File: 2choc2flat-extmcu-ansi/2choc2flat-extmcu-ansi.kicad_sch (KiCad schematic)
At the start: 142 parts, among them J1 Conn_01x09_Male, J2 Conn_01x05_Male, J3 Conn_01x09_Male, K1 KEYSW, K10 KEYSW, K11 KEYSW, K12 KEYSW, K13 KEYSW, K14 KEYSW, K16 KEYSW, K17 KEYSW, K18 KEYSW, K19 KEYSW, K2 KEYSW, K20 KEYSW, K21 KEYSW, K22 KEYSW, K23 KEYSW, K24 KEYSW, K25 KEYSW, K26 KEYSW, K27 KEYSW, K28 KEYSW, K29 KEYSW, K3 KEYSW, K31 KEYSW, K31-1 KEYSW, K32 KEYSW, K33 KEYSW, K34 KEYSW, K35 KEYSW, K36 KEYSW, K37 KEYSW, K38 KEYSW, K39 KEYSW, K4 KEYSW, K40 KEYSW, K41 KEYSW, K42 KEYSW, K44 KEYSW, K46 KEYSW, K47 KEYSW, K48 KEYSW, K49 KEYSW, K5 KEYSW, K50 KEYSW, K51 KEYSW, K52 KEYSW, K53 KEYSW, K54 KEYSW, K55 KEYSW, K56 KEYSW, K57 KEYSW, K58 KEYSW, K59 KEYSW, K6 KEYSW, K61 KEYSW, K62 KEYSW, K63 KEYSW, K67 KEYSW, K7 KEYSW, K71 KEYSW, K72 KEYSW, K73 KEYSW, K74 KEYSW, K75 KEYSW, K8 KEYSW, K9 KEYSW

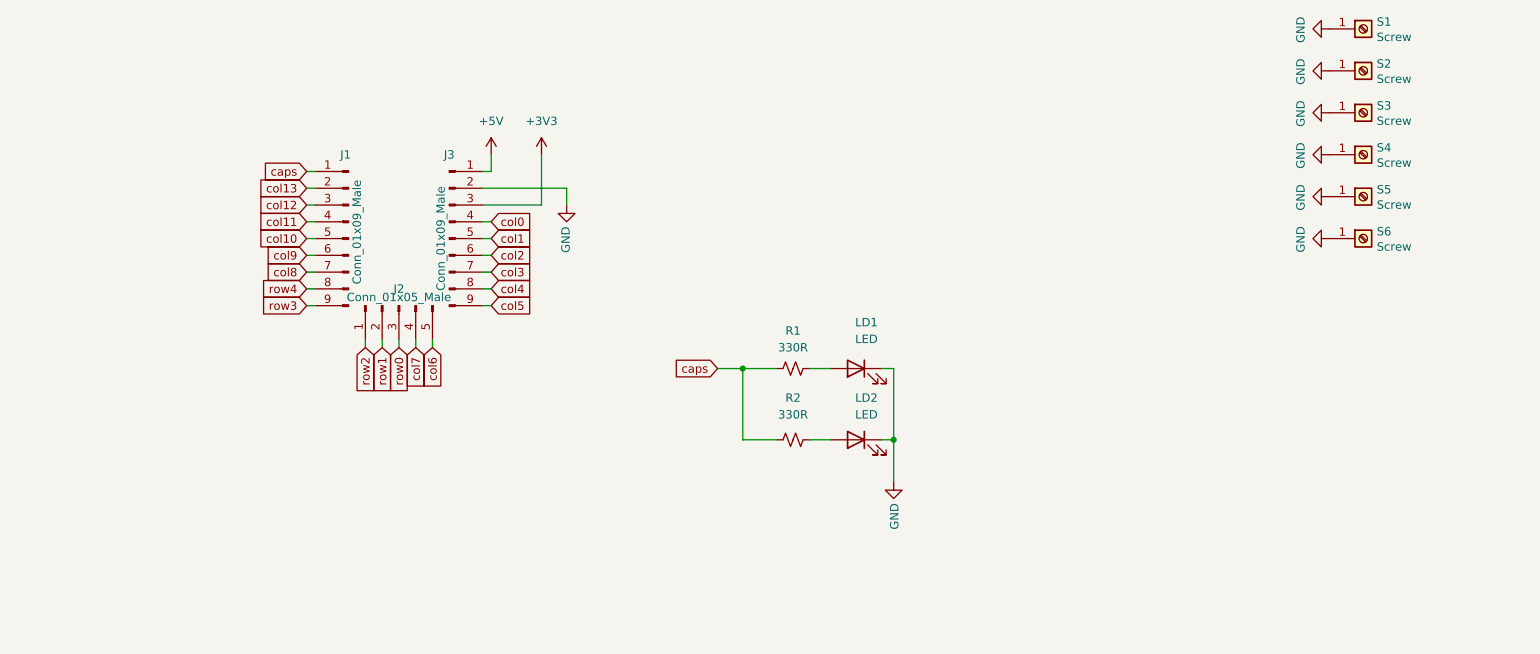
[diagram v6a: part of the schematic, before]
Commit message: v1.5 ANSI with SMD rp2040 tiny
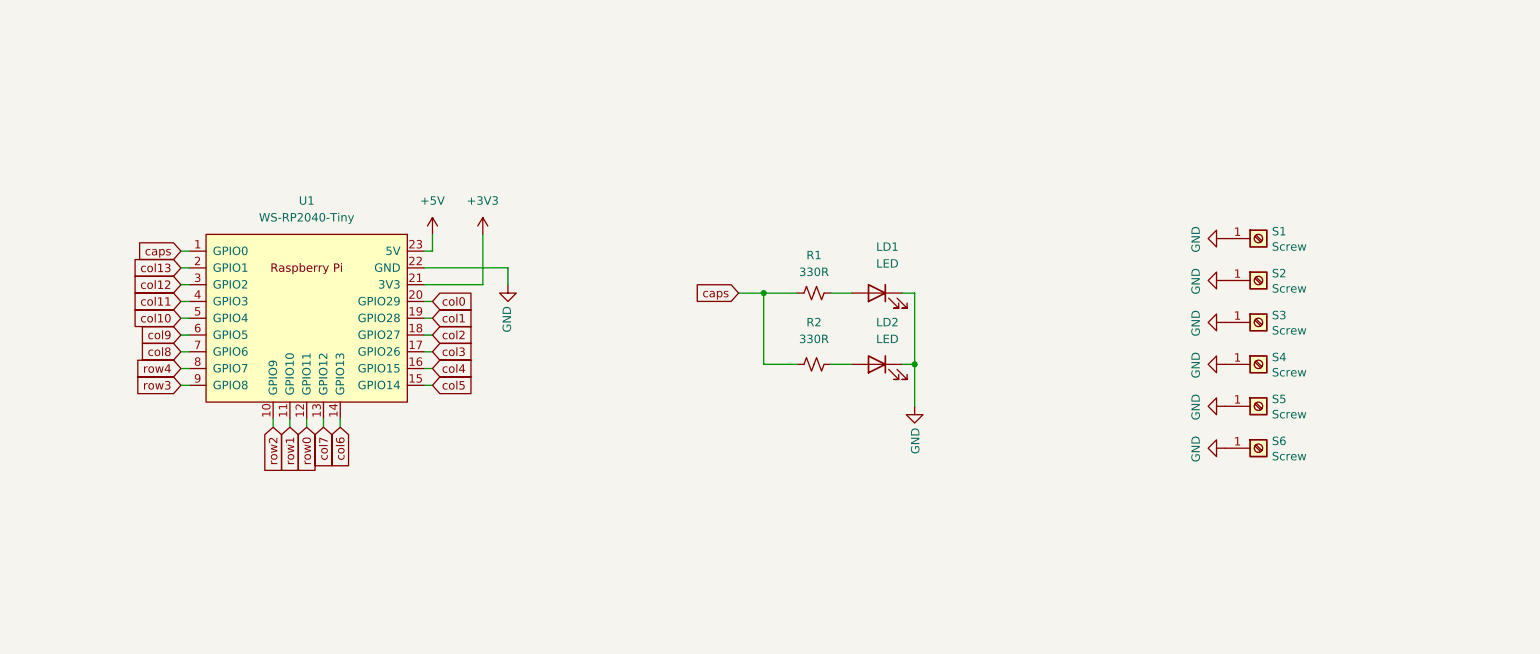
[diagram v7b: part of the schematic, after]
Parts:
- removed J1, J3: Conn_01x09_Male, Connector_PinHeader_2.54mm:PinHeader_1x09_P2.54mm_Vertical, symbol Connector:Conn_01x09_Male
- removed J2: Conn_01x05_Male, Connector_PinHeader_2.54mm:PinHeader_1x05_P2.54mm_Vertical, symbol Connector:Conn_01x05_Male
- added U1: WS-RP2040-Tiny, schizobovine:WAVESHARE_RP2040_TINY, symbol schizobovine:WS-RP2040-Tiny
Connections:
- net +3V3: now also U1.21 (3V3)
- net +5V: now also U1.23 (5V)
- net GND: now also U1.22 (GND)
- net caps: now also U1.1 (GPIO0)
- net col0: now also U1.20 (GPIO29)
- net col1: now also U1.19 (GPIO28)
- net col10: now also U1.5 (GPIO4)
- net col11: now also U1.4 (GPIO3)
- net col12: now also U1.3 (GPIO2)
- net col13: now also U1.2 (GPIO1)
- net col2: now also U1.18 (GPIO27)
- net col3: now also U1.17 (GPIO26)
- net col4: now also U1.16 (GPIO15)
- net col5: now also U1.15 (GPIO14)
- net col6: now also U1.14 (GPIO13)
- net col7: now also U1.13 (GPIO12)
- net col8: now also U1.7 (GPIO6)
- net col9: now also U1.6 (GPIO5)
- net row0: now also U1.12 (GPIO11)
- net row1: now also U1.11 (GPIO10)
- net row2: now also U1.10 (GPIO9)
- net row3: now also U1.9 (GPIO8)
- net row4: now also U1.8 (GPIO7)
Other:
- moved on the sheet: LD1, LD2, R1, R2, S1, S2, S3, S4, S5, S6

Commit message: update ANSI for foam
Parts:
- K31: footprint Switch_Keyboard_Hotswap_Kailh_mine:SW_Hotswap_Kailh_Choc_V2_1.75u -> Switch_Keyboard_Hotswap_Kailh_mine:SW_Hotswap_Kailh_Choc_V2_1.75u_capslock
- K31-1: footprint Switch_Keyboard_Hotswap_Kailh_mine:SW_Hotswap_Kailh_Choc_V2_1.25u -> Switch_Keyboard_Hotswap_Kailh_mine:SW_Hotswap_Kailh_Choc_V2_1.25u_capslock
- K67: footprint Switch_Keyboard_Hotswap_Kailh_mine:SW_Hotswap_Kailh_Choc_V2_6.25u -> Switch_Keyboard_Hotswap_Kailh_mine:SW_Hotswap_Kailh_Choc_V2_6.25u_special2
